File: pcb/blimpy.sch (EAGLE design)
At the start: 74 parts, among them J4 3-PIN SMD, J5 3-PIN SMD, J6 3-PIN SMD, J7 3-PIN SMD, Q1 mmbt2222, Q2 mmbt2222, Q3 DMG3415U, U1 RGB, U10 MAX17048, U2 AP2112-3.3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

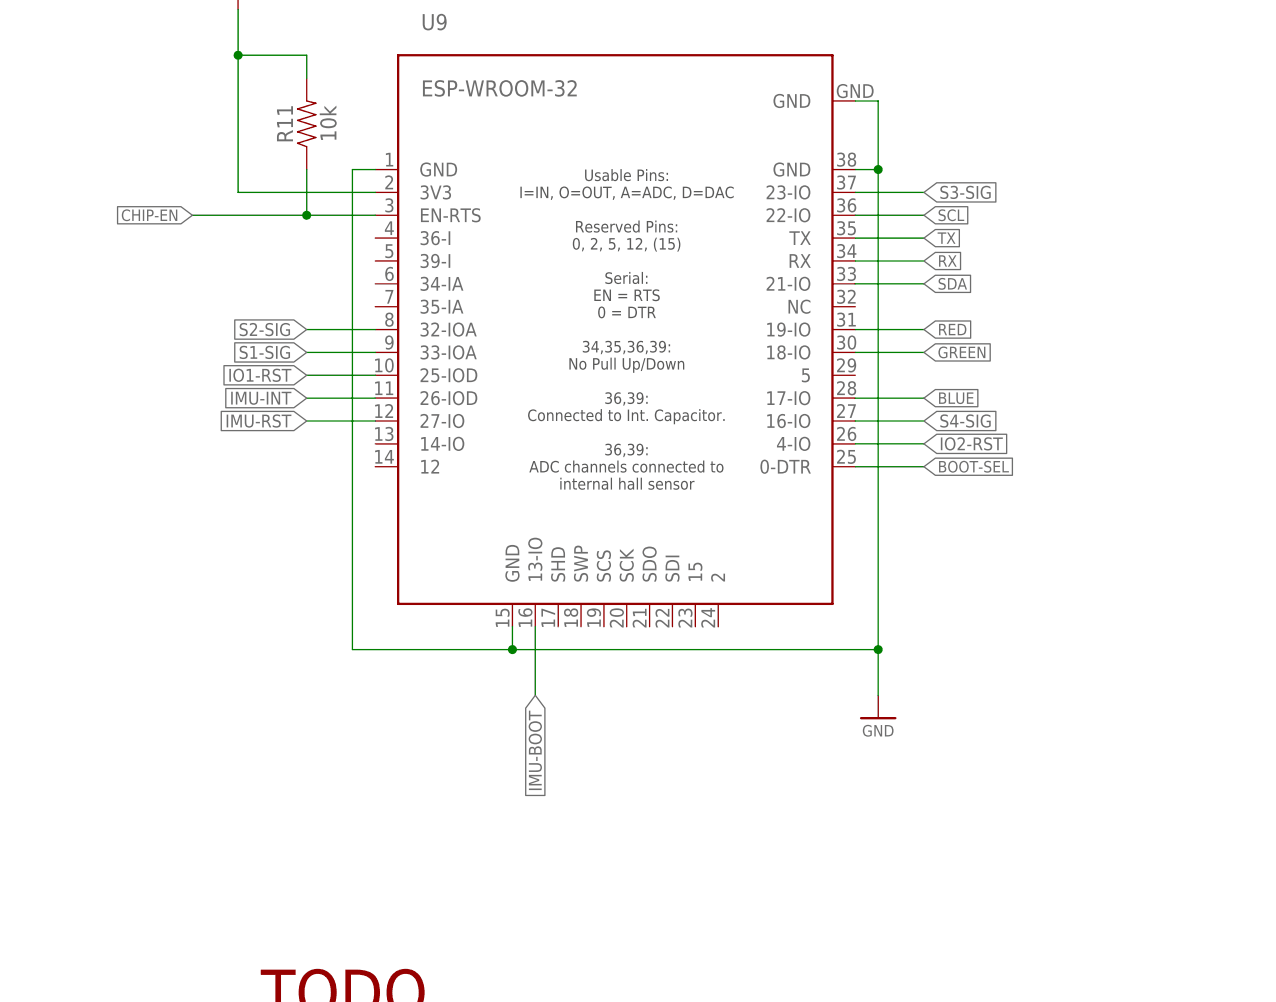
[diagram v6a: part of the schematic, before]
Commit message: added esp32 pogo pins
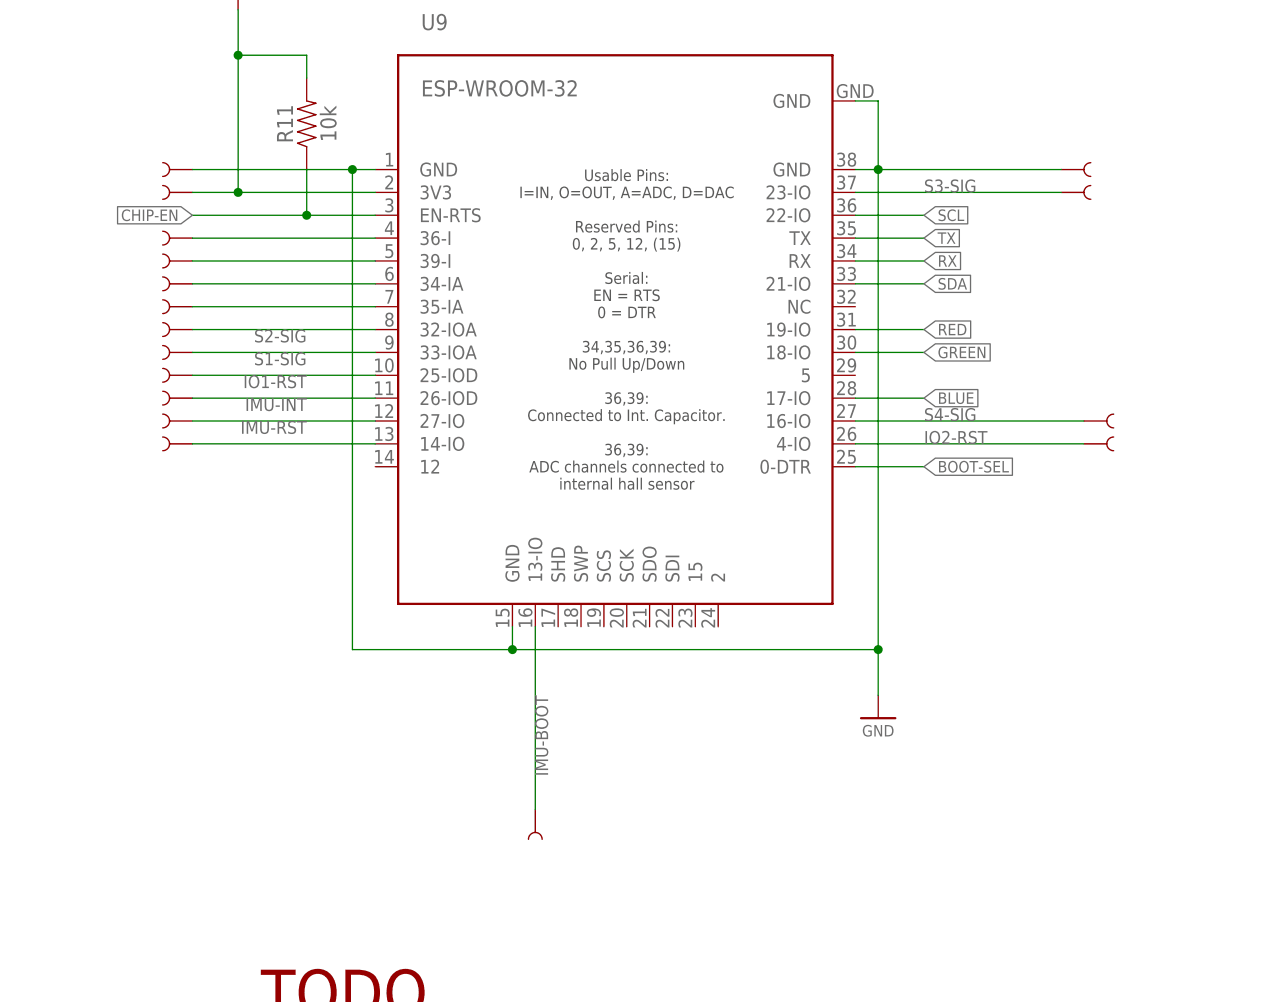
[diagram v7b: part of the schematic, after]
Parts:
- added TP1, TP10, TP11, TP12, TP13, TP14, TP15, TP16, TP17, TP2, TP3, TP4, TP5, TP6, TP7, TP8, TP9: TEST-POINT3, SparkFun-Connectors:TEST-POINT3
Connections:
- new net N$18: TP10.1, U9.36-I
- new net N$19: TP9.1, U9.39-I
- new net N$20: TP8.1, U9.34-IA
- new net N$21: TP7.1, U9.35-IA
- new net N$22: TP6.1, U9.14-IO
- net 3.3V: now also TP11.1
- net GND: now also TP12.1, TP13.1
- net IMU-BOOT: now also TP17.1
- net IMU-INT: now also TP4.1
- net IMU-RST: now also TP5.1
- net IO1-RST: now also TP3.1
- net IO2-RST: now also TP16.1
- net S1-SIG: now also TP2.1
- net S2-SIG: now also TP1.1
- net S3-SIG: now also TP14.1
- net S4-SIG: now also TP15.1

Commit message: updated todo
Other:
- note added: "TODO - Check all components"
- note removed: "TODO - Expose unused GPIOs - Expose important GPIOs - Check all components"
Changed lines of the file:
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@@
 <text x="378.46" y="185.42" size="1.27" layer="97">INT OSC</text>
 <text x="160.02" y="-58.42" size="5.08" layer="94" align="top-left">TODO
-- Expose unused GPIOs
-- Expose important GPIOs
 - Check all components</text>
 <text x="342.9" y="106.68" size="1.778" layer="94">GPIO Expander 1
